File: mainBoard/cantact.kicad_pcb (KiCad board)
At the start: 2 copper layers, 36.1 x 59.9 mm, 45 parts, among them J1 Cantact, P2 SWD, P4 USB_C_Plug_USB2.0, U1 STM32F042C6T6, U3 MCP2551-I/SN, U4 XC6220B331MR-G, Y1 16 Mhz

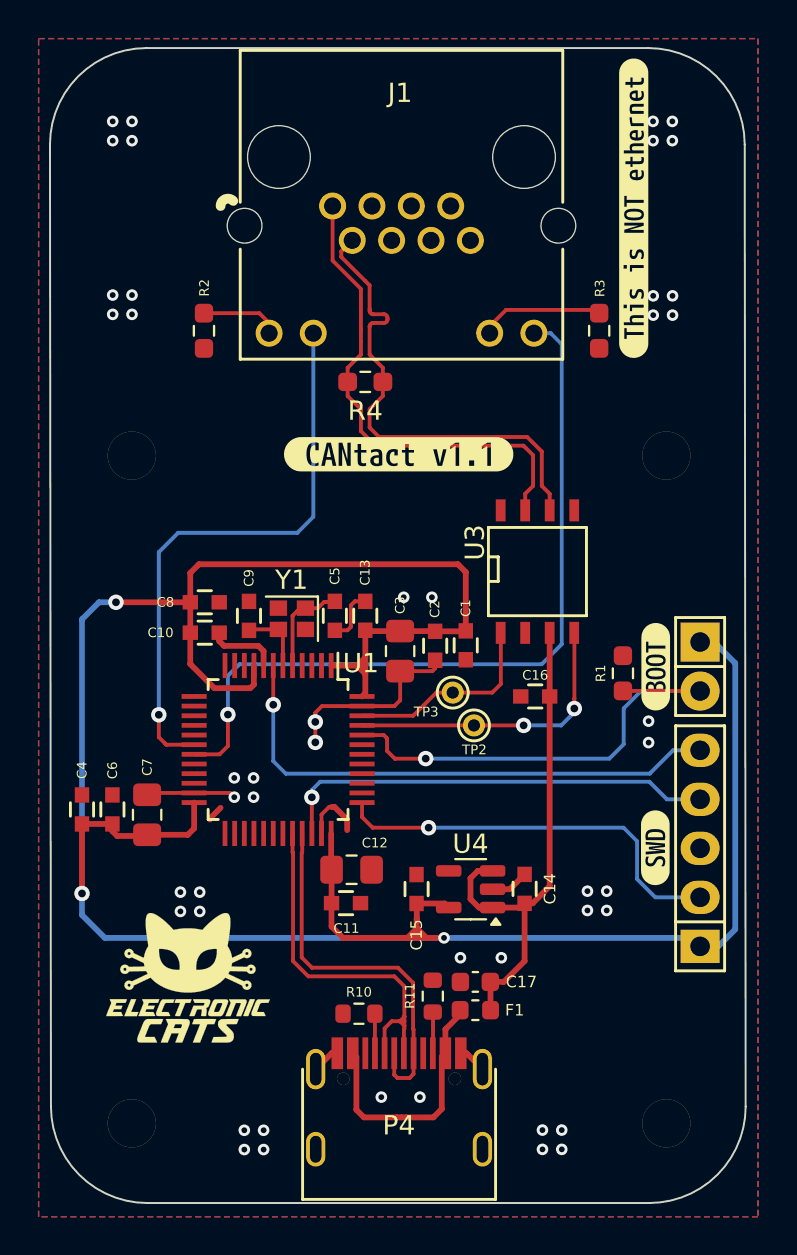
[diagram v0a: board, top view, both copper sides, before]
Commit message: feat(Hw):Update_Labels_And_BOM
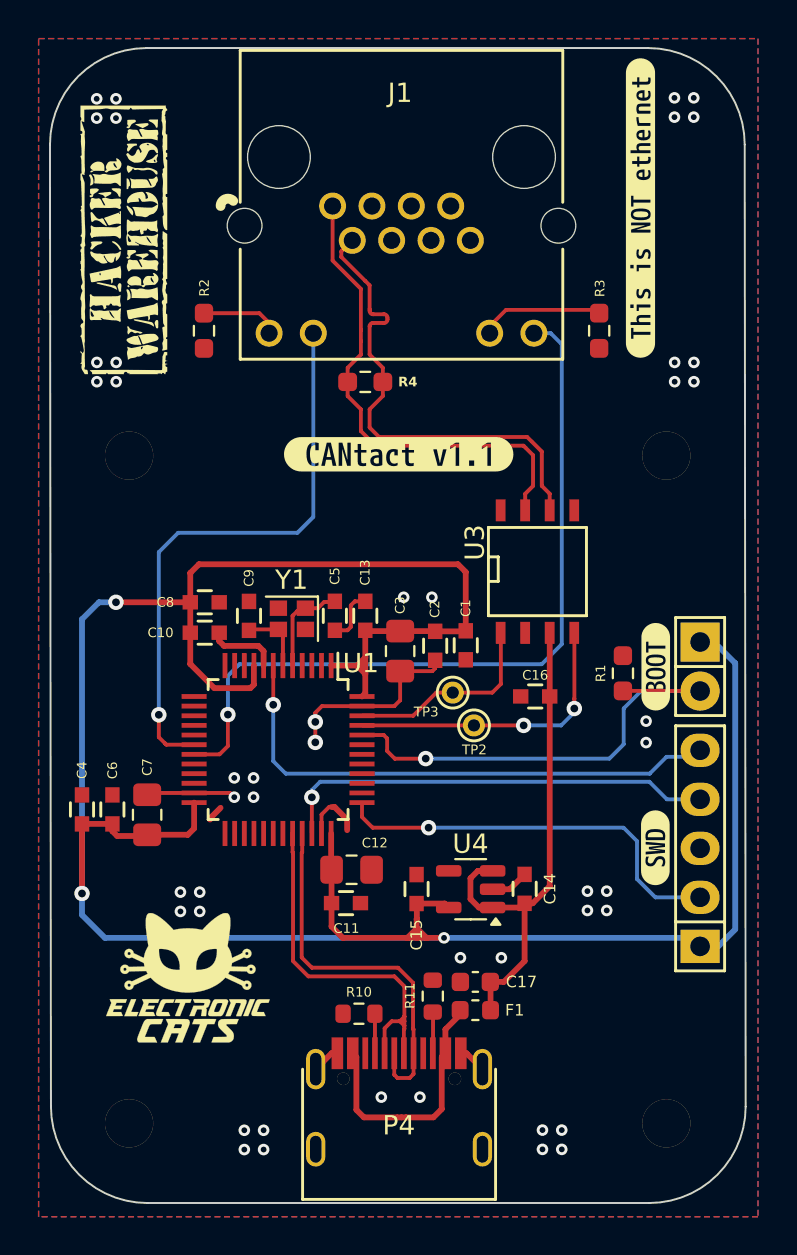
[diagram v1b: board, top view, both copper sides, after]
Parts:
- moved kibuzzard-68FBE69F 0.35 mm to (154.8, 100.5)
- moved ? 0.14 mm to (128.3, 113.3)
- moved ? 0.14 mm to (128.3, 147.9)

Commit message: feat: logo adjust
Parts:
- removed kibuzzard-68FBE69F: G***, kibuzzard-68FBE69F
- added kibuzzard-68FBE702: G***, kibuzzard-68FBE702, F.Cu at (155.3, 102.5)
- added kibuzzard-68FFF13A: G***, kibuzzard-68FFF13A, B.Cu at (142.1, 94.3)
- moved kibuzzard-68FBE702 16.7 mm to (129.5, 102.7), turned to 90 degrees

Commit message: feat:update v1.2
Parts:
- removed kibuzzard-68FBE702 (x2): G***, kibuzzard-68FBE702
- removed kibuzzard-68FBE735: G***, kibuzzard-68FBE735
- added kibuzzard-68FFF3A1: G***, kibuzzard-68FFF3A1, F.Cu at (129.5, 102.7)
- added kibuzzard-68FFF3A9: G***, kibuzzard-68FFF3A9, F.Cu at (155.3, 102.5)
- added kibuzzard-68FFF3B2: G***, kibuzzard-68FFF3B2, B.Cu at (142.4, 122.0)

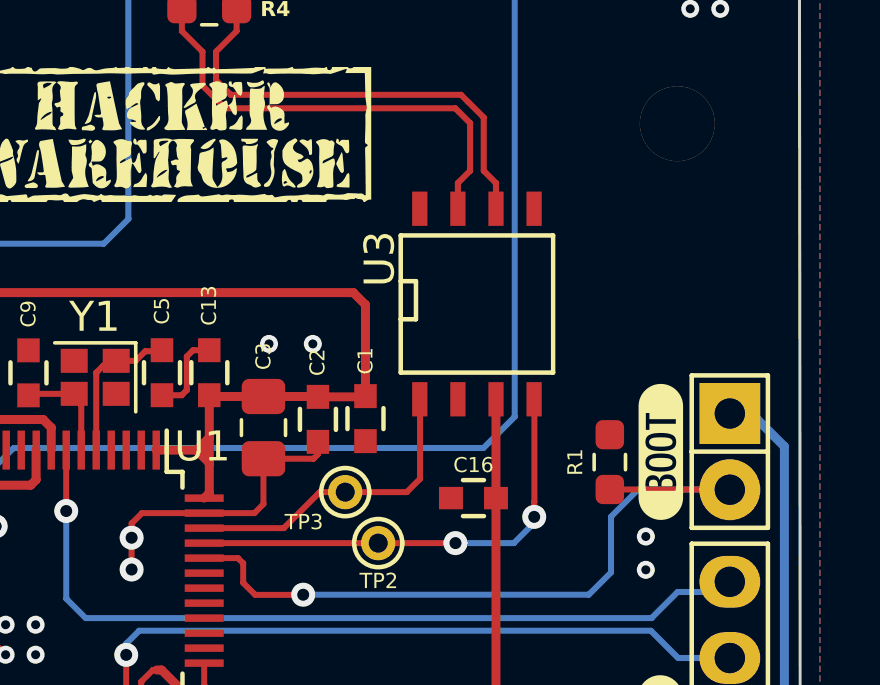
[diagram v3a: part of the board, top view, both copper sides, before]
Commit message: fix: change footprint
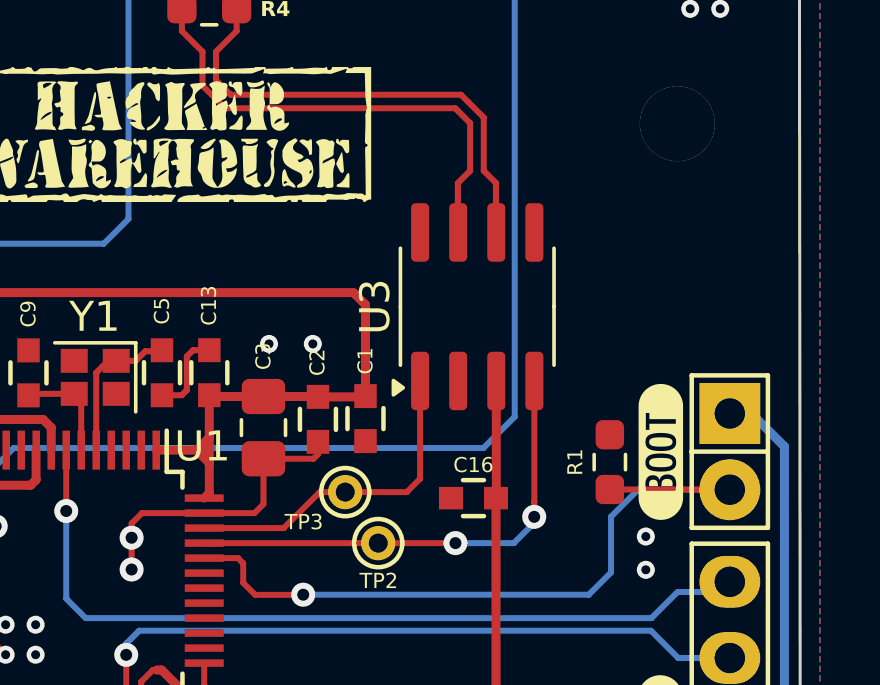
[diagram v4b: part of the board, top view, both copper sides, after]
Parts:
- U3: footprint SMD_Packages:SOIC-8-N -> Package_SO:SOIC-8_3.9x4.9mm_P1.27mm
- moved U3 0.09 mm to (149.5, 119.4), turned to 90 degrees
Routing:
- net /CAN+: track 25.4 -> 27.0 mm
- net /CAN_TX: track 10.5 -> 11.8 mm
- net /CAN_RX: track 15.4 -> 16.6 mm
- net /CAN-: track 25.3 -> 26.1 mm
